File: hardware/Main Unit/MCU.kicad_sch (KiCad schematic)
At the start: 35 parts, among them J1 3221-10-0300-00, SW1 MJTP1243, SW2 MJTP1243, U1 MCXN547VKLT, X1 24.0000MHz

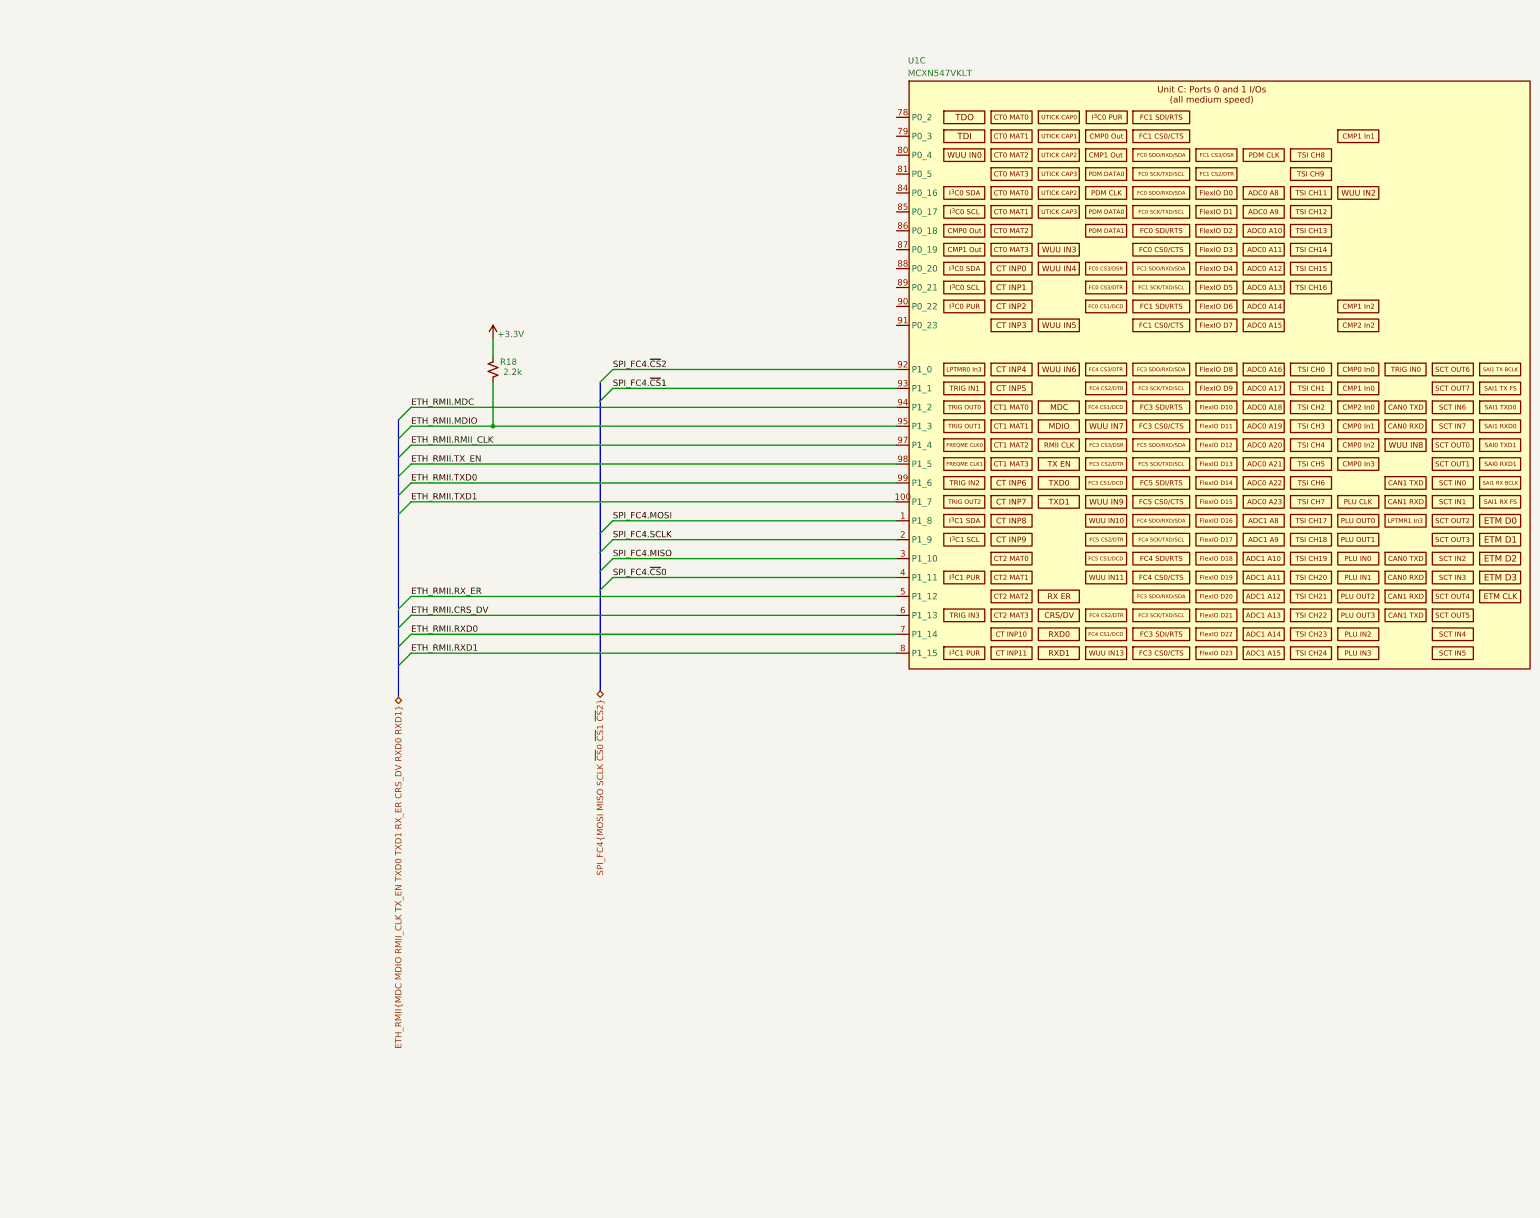
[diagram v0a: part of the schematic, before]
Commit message: Implement card connector schematic
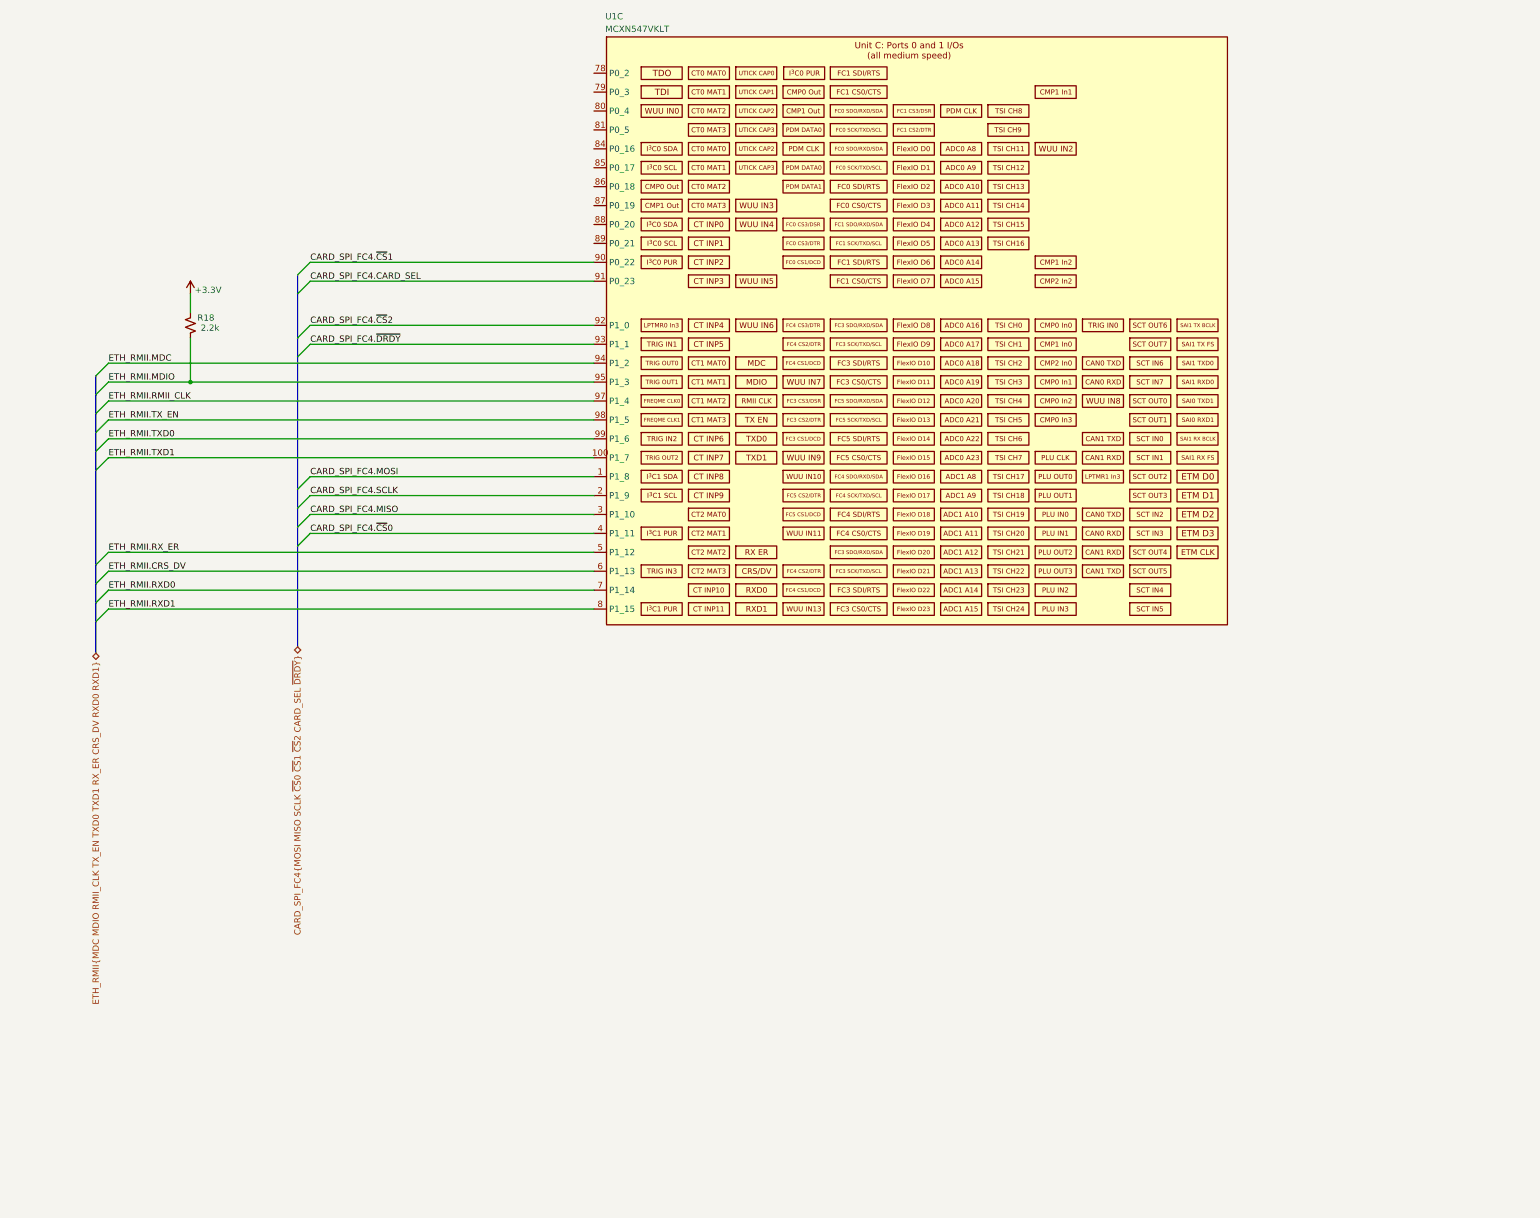
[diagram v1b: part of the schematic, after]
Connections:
- net CARD_SPI_FC4.~{CS}1: now reaches U1.90 (P0_22)
- net CARD_SPI_FC4.CARD_SEL: now reaches U1.91 (P0_23)
- net SPI_FC4.MISO renamed CARD_SPI_FC4.MISO
- net SPI_FC4.MOSI renamed CARD_SPI_FC4.MOSI
- net SPI_FC4.SCLK renamed CARD_SPI_FC4.SCLK
- net SPI_FC4.~{CS}0 renamed CARD_SPI_FC4.~{CS}0
- net SPI_FC4.~{CS}1 renamed CARD_SPI_FC4.~{DRDY}
- net SPI_FC4.~{CS}2 renamed CARD_SPI_FC4.~{CS}2
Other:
- moved on the sheet: R18, U1C

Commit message: Add MicroSD card, finish MCU symbol
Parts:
- added C27: 100nF, Capacitor_SMD:C_0603_1608Metric, symbol Device:C_Small
- added unit 5 of U1
- added unit 4 of U1
- added unit 7 of U1
- added unit 6 of U1
- J1: footprint Project Library:3221-10-0300-00 -> ProjectLibrary:3221-10-0300-00
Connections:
- net +3.3V: now also U1.73 (VDD_P3), C27.1
- net GND: now also U1.43 (VSS), C27.2
- net CARD_SPI_FC7.~{CS}1: now reaches U1.78 (P0_2)
- net CARD_SPI_FC7.~{CS}2: now reaches U1.79 (P0_3)
- net at R1.2: now also U1.9 (RESET_B); no longer U1.12 (RESET_B)
- new net CARD_SPI_FC7.CARD_SEL: U1.50 (P5_2)
- new net CARD_SPI_FC7.MISO: U1.69 (P3_9)
- new net CARD_SPI_FC7.MOSI: U1.70 (P3_8)
- new net CARD_SPI_FC7.SCLK: U1.71 (P3_7)
- new net CARD_SPI_FC7.~{CS}0: U1.65 (P3_12)
- new net CARD_SPI_FC7.~{DRDY}: U1.51 (P5_3)
- new net CARD_SPI_FC8.CARD_SEL: U1.64 (P3_13)
- new net CARD_SPI_FC8.MISO: U1.61 (P3_16)
- new net CARD_SPI_FC8.MOSI: U1.63 (P3_14)
- new net CARD_SPI_FC8.SCLK: U1.62 (P3_15)
- new net CARD_SPI_FC8.~{CS}0: U1.60 (P3_17)
- new net CARD_SPI_FC8.~{CS}1: U1.57 (P3_20)
- new net CARD_SPI_FC8.~{CS}2: U1.56 (P3_21)
- new net CARD_SPI_FC8.~{DRDY}: U1.75 (P3_0)
- new net CARD_SPI_FC9.CARD_SEL: U1.15 (P2_1)
- new net CARD_SPI_FC9.MISO: U1.19 (P2_5)
- new net CARD_SPI_FC9.MOSI: U1.18 (P2_4)
- new net CARD_SPI_FC9.SCLK: U1.17 (P2_3)
- new net CARD_SPI_FC9.~{CS}0: U1.16 (P2_2)
- new net CARD_SPI_FC9.~{CS}1: U1.14 (P2_0)
- new net CARD_SPI_FC9.~{CS}2: U1.21 (P2_7)
- new net CARD_SPI_FC9.~{DRDY}: U1.20 (P2_6)
- new net uSD_SPI_FC6.MISO: U1.68 (P3_10)
- new net uSD_SPI_FC6.MOSI: U1.74 (P3_1)
- new net uSD_SPI_FC6.SCLK: U1.72 (P3_6)
- new net uSD_SPI_FC6.~{CS}: U1.67 (P3_11)
- no-connect marks 7 -> 5
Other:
- moved on the sheet: C4, C5, C6, C8

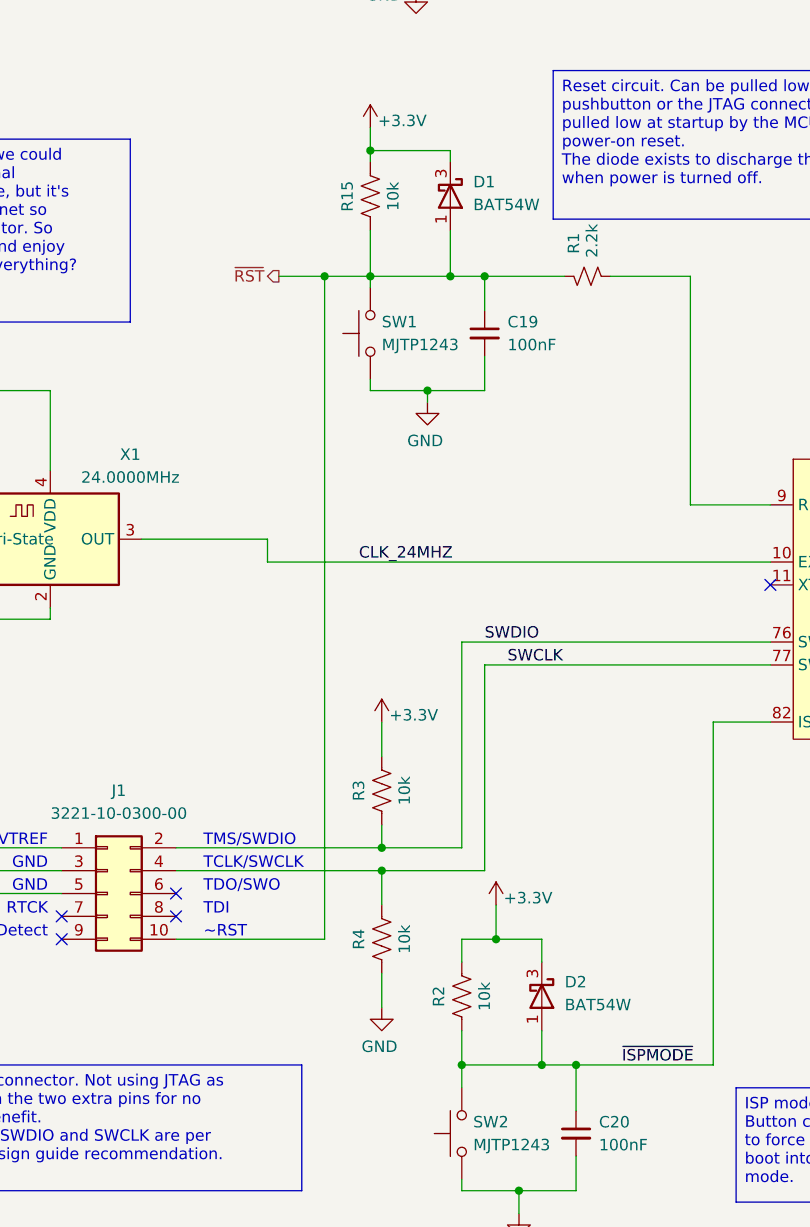
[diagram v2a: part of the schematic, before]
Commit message: Start on Digital IO card
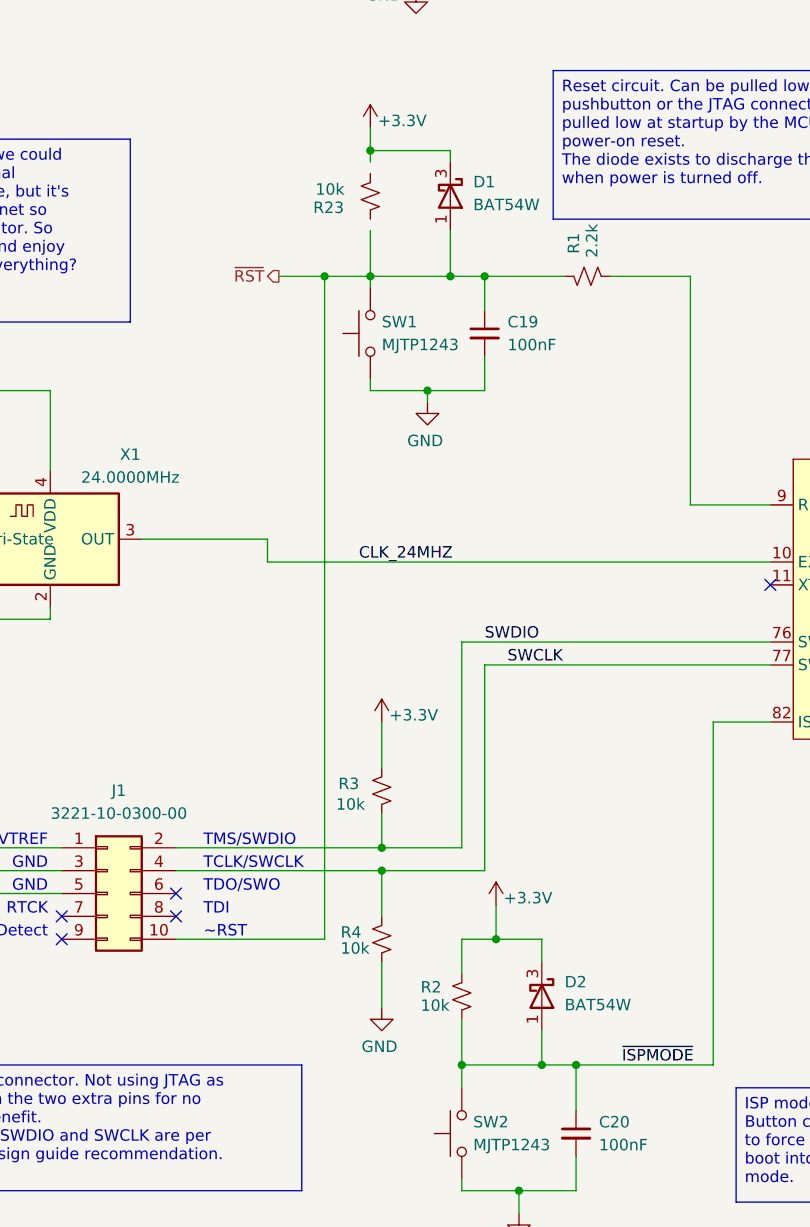
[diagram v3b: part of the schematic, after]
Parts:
- removed R15, R2, R3, R4: 10k, Resistor_SMD:R_1206_3216Metric, symbol Device:R_US
- added R2, R23, R3, R4: 10k, Resistor_SMD:R_0603_1608Metric, symbol Device:R_Small_US
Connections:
- net +3.3V: now also R2.2, R3.2
- net GND: now also R4.1
- net SWCLK: now also R4.2
- net SWDIO: now also R3.1
- net ~{ISPMODE}: now also R2.1

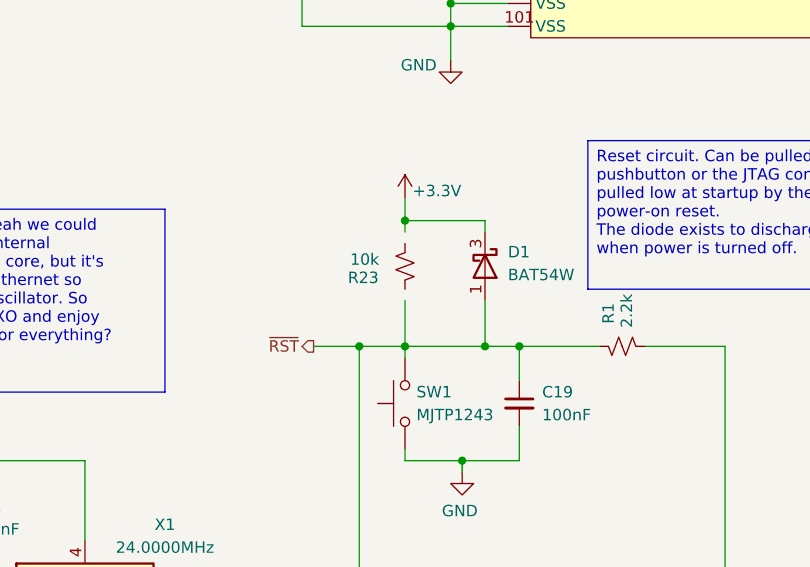
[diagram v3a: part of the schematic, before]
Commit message: MCU schematic tweaks
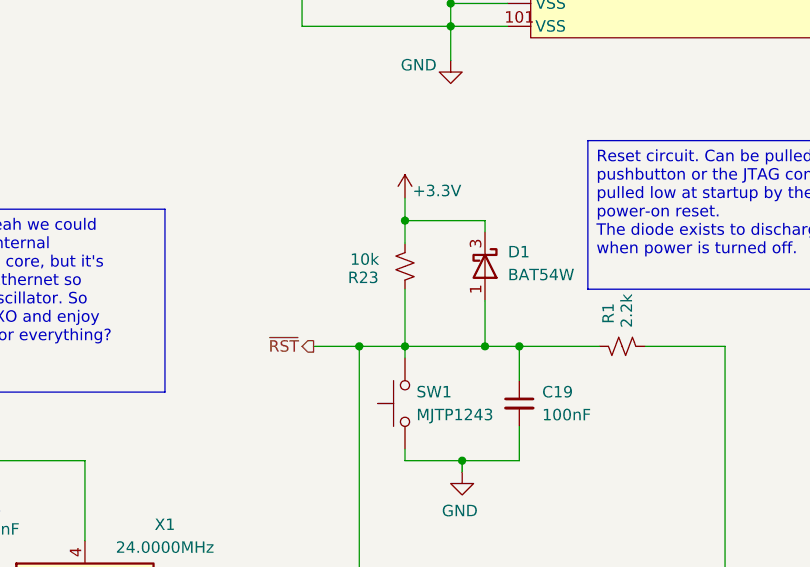
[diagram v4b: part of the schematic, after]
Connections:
- net +3.3V: now also R23.2
- net ~{RST}: now also R23.1
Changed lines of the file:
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@@
+	(wire
+		(pts
+			(xy 82.55 182.88) (xy 82.55 189.23)
+		)
+		(stroke
+			(width 0)
+			(type default)
+		)
+	)
 	(wire
 		(pts
@@
 		)
 	)
+	(wire
+		(pts
+			(xy 82.55 175.26) (xy 82.55 177.8)
+		)
+		(stroke
+			(width 0)
+			(type default)
+		)
+	)
 	(bus
 		(pts
@@
 	(wire
 		(pts
-			(xy 82.55 184.15) (xy 82.55 189.23)
-		)
-		(stroke
-			(width 0)
-			(type default)
-		)
-	)
-	(wire
-		(pts
 			(xy 83.82 255.27) (xy 95.25 255.27)
 		)
@@
 		)
 		(stroke
-			(width 0)
-			(type default)
-		)
-	)
-	(wire
-		(pts
-			(xy 82.55 175.26) (xy 82.55 176.53)
-		)
-		(stroke
